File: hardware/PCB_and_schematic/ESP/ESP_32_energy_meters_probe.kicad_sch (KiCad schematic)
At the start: 33 parts, among them J2 EXTERNAL_SIGNALS, J5 METER_GRID, J9 METER_PV, U4 ST485EBDR, U5 ST485EBDR, U6 74HC14

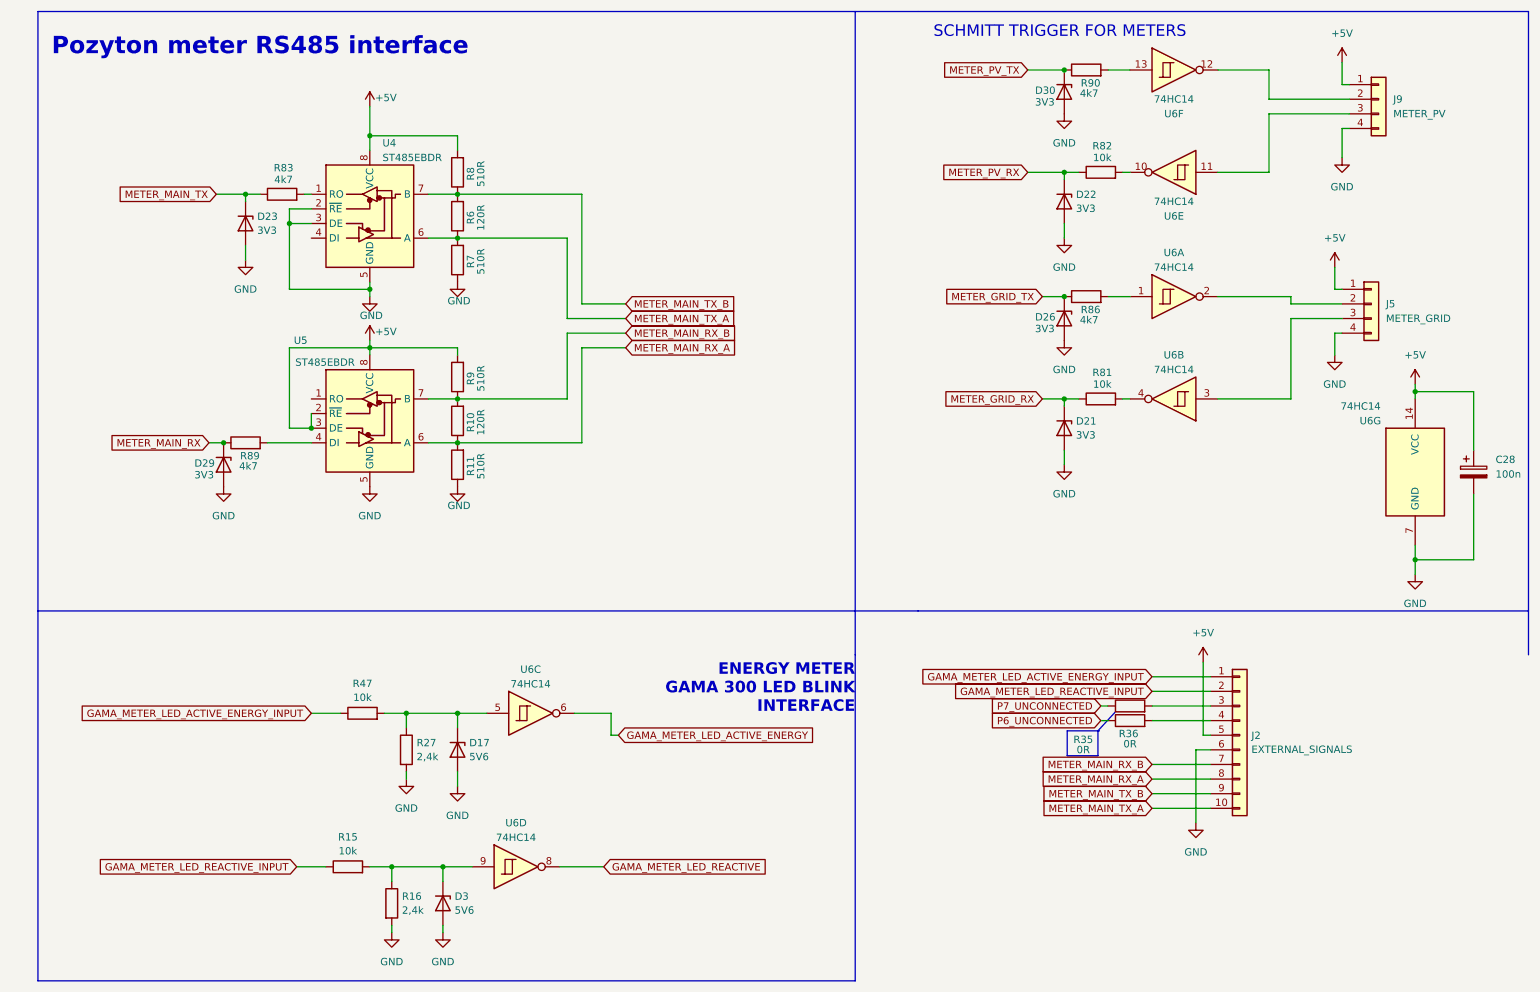
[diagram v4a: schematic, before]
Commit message: ESP PCB Route progress
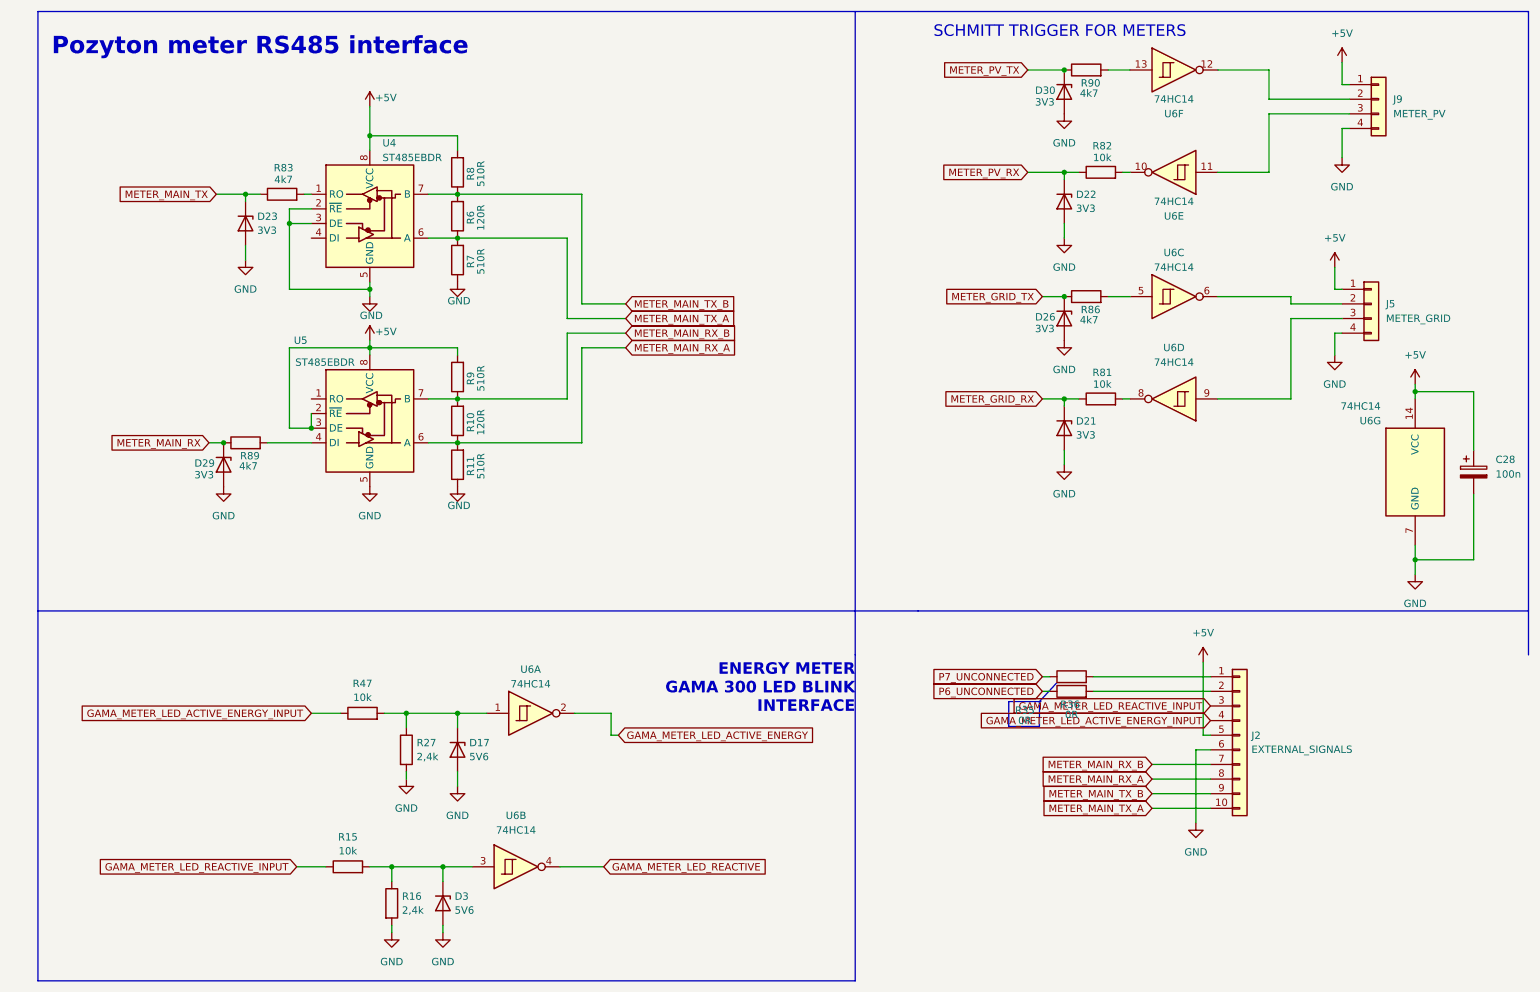
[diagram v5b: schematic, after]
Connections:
- net GAMA_METER_LED_ACTIVE_ENERGY: now also U6.2; no longer U6.6
- net GAMA_METER_LED_ACTIVE_ENERGY_INPUT: now also J2.4 (Pin_4); no longer J2.1 (Pin_1)
- net GAMA_METER_LED_REACTIVE: now also U6.4; no longer U6.8
- net GAMA_METER_LED_REACTIVE_INPUT: now also J2.3 (Pin_3); no longer J2.2 (Pin_2)
- net at D17.1 (K), R27.1, R47.2: now also U6.1; no longer U6.5
- net at R35.2: now also J2.1 (Pin_1); no longer J2.3 (Pin_3)
- net at R36.2: now also J2.2 (Pin_2); no longer J2.4 (Pin_4)
- net at U6.3: now also D3.1 (K), R15.2, R16.1; no longer J5.3 (Pin_3)
- net at R81.2: now also U6.8; no longer U6.4
- net at R86.2: now also U6.5; no longer U6.1
- net at J5.2 (Pin_2): now also U6.6; no longer U6.2
- new net: J5.3 (Pin_3), U6.9
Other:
- moved on the sheet: R35, R36, U6A, U6B, U6C, U6D
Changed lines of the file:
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@@
 	(wire
 		(pts
-			(xy 215.9 140.97) (xy 226.06 140.97)
-		)
-		(stroke
-			(width 0)
-			(type default)
-		)
-	)
-	(wire
-		(pts
 			(xy 236.22 45.72) (xy 227.33 45.72)
 		)
@@
 	(wire
 		(pts
-			(xy 215.9 133.35) (xy 226.06 133.35)
+			(xy 205.74 133.35) (xy 226.06 133.35)
 		)
 		(stroke
@@
 	(wire
 		(pts
-			(xy 215.9 138.43) (xy 226.06 138.43)
-		)
-		(stroke
-			(width 0)
-			(type default)
-		)
-	)
-	(wire
-		(pts
 			(xy 58.42 58.42) (xy 58.42 60.96)
 		)
@@
 	(wire
 		(pts
-			(xy 207.01 140.97) (xy 208.28 140.97)
+			(xy 196.85 135.89) (xy 198.12 135.89)
 		)
 		(stroke
@@
 	(polyline
 		(pts
-			(xy 206.502 142.748) (xy 209.55 139.446)
+			(xy 196.342 137.668) (xy 199.39 134.366)
 		)
 		(stroke
@@
 	(wire
 		(pts
-			(xy 207.01 138.43) (xy 208.28 138.43)
+			(xy 196.85 133.35) (xy 198.12 133.35)
 		)
 		(stroke
@@
 	(polyline
 		(pts
-			(xy 206.756 142.748) (xy 206.502 142.748)
+			(xy 196.596 137.668) (xy 196.342 137.668)
 		)
 		(stroke
@@
 	(wire
 		(pts
-			(xy 215.9 135.89) (xy 226.06 135.89)
+			(xy 205.74 135.89) (xy 226.06 135.89)
 		)
 		(stroke
@@
 	)
 	(rectangle
-		(start 201.168 142.748)
-		(end 206.502 147.066)
+		(start 191.008 137.668)
+		(end 196.342 141.986)
 		(stroke
 			(width 0)
@@
 	(global_label "GAMA_METER_LED_ACTIVE_ENERGY_INPUT"
 		(shape input)
-		(at 215.9 133.35 180)
+		(at 226.06 140.97 180)
 		(fields_autoplaced yes)
 		(effects
@@
 		)
 		(property "Intersheetrefs" "${INTERSHEET_REFS}"
-			(at 174.815 133.35 0)
+			(at 184.975 140.97 0)
 			(effects
 				(font
@@
 	(global_label "GAMA_METER_LED_REACTIVE_INPUT"
 		(shape input)
-		(at 215.9 135.89 180)
+		(at 226.06 138.43 180)
 		(fields_autoplaced yes)
 		(effects
@@
 		)
 		(property "Intersheetrefs" "${INTERSHEET_REFS}"
-			(at 180.6207 135.89 0)
+			(at 190.7807 138.43 0)
 			(effects
 				(font
@@
 	(global_label "P7_UNCONNECTED"
 		(shape input)
-		(at 207.01 138.43 180)
+		(at 196.85 133.35 180)
 		(fields_autoplaced yes)
 		(effects
@@
 		)
 		(property "Intersheetrefs" "${INTERSHEET_REFS}"
-			(at 186.8496 138.43 0)
+			(at 176.6896 133.35 0)
 			(effects
 				(font
@@
 	(global_label "P6_UNCONNECTED"
 		(shape input)
-		(at 207.01 140.97 180)
+		(at 196.85 135.89 180)
 		(fields_autoplaced yes)
 		(effects
@@
 		)
 		(property "Intersheetrefs" "${INTERSHEET_REFS}"
-			(at 186.8496 140.97 0)
+			(at 176.6896 135.89 0)
 			(effects
 				(font
@@
 	(symbol
 		(lib_id "74xx:74HC14")
-		(at 219.71 85.09 180)
+		(at 105.41 166.37 0)
 		(unit 2)
 		(exclude_from_sim no)
@@
 		(fields_autoplaced yes)
 		(property "Reference" "U6"
-			(at 219.71 77.47 0)
+			(at 105.41 157.48 0)
 			(effects
 				(font
@@
 		)
 		(property "Value" "74HC14"
-			(at 219.71 80.01 0)
+			(at 105.41 160.02 0)
 			(effects
 				(font
@@
 		)
 		(property "Footprint" "Package_SO:SOIC-14_3.9x8.7mm_P1.27mm"
-			(at 219.71 85.09 0)
+			(at 105.41 166.37 0)
 			(effects
 				(font
@@
 		)
 		(property "Datasheet" "http://www.ti.com/lit/gpn/sn74HC14"
-			(at 219.71 85.09 0)
+			(at 105.41 166.37 0)
 			(effects
 				(font
@@
 		)
 		(property "Description" "Hex inverter schmitt trigger"
-			(at 219.71 85.09 0)
+			(at 105.41 166.37 0)
 			(effects
 				(font
@@
 	(symbol
 		(lib_id "74xx:74HC14")
-		(at 107.95 139.7 0)
+		(at 219.71 67.31 0)
 		(unit 3)
 		(exclude_from_sim no)
@@
 		(fields_autoplaced yes)
 		(property "Reference" "U6"
-			(at 107.95 132.08 0)
+			(at 219.71 59.69 0)
 			(effects
 				(font
@@
 		)
 		(property "Value" "74HC14"
-			(at 107.95 134.62 0)
+			(at 219.71 62.23 0)
 			(effects
 				(font
@@
 		)
 		(property "Footprint" "Package_SO:SOIC-14_3.9x8.7mm_P1.27mm"
-			(at 107.95 139.7 0)
+			(at 219.71 67.31 0)
 			(effects
 				(font
@@
 		)
 		(property "Datasheet" "http://www.ti.com/lit/gpn/sn74HC14"
-			(at 107.95 139.7 0)
+			(at 219.71 67.31 0)
 			(effects
 				(font
@@
 		)
 		(property "Description" "Hex inverter schmitt trigger"
-			(at 107.95 139.7 0)
+			(at 219.71 67.31 0)
 			(effects
 				(font
@@
 	(symbol
 		(lib_id "74xx:74HC14")
-		(at 105.41 166.37 0)
+		(at 219.71 85.09 180)
 		(unit 4)
 		(exclude_from_sim no)
@@
 		(fields_autoplaced yes)
 		(property "Reference" "U6"
-			(at 105.41 158.75 0)
+			(at 219.71 76.2 0)
 			(effects
 				(font
@@
 		)
 		(property "Value" "74HC14"
-			(at 105.41 161.29 0)
+			(at 219.71 78.74 0)
 			(effects
 				(font
@@
 		)
 		(property "Footprint" "Package_SO:SOIC-14_3.9x8.7mm_P1.27mm"
-			(at 105.41 166.37 0)
+			(at 219.71 85.09 0)
 			(effects
 				(font
@@
 		)
 		(property "Datasheet" "http://www.ti.com/lit/gpn/sn74HC14"
-			(at 105.41 166.37 0)
+			(at 219.71 85.09 0)
 			(effects
 				(font
@@
 		)
 		(property "Description" "Hex inverter schmitt trigger"
-			(at 105.41 166.37 0)
+			(at 219.71 85.09 0)
 			(effects
 				(font
@@
 	(symbol
 		(lib_id "Device:R")
-		(at 212.09 138.43 90)
+		(at 201.93 133.35 90)
 		(unit 1)
 		(exclude_from_sim no)
@@
 		(dnp no)
 		(property "Reference" "R35"
-			(at 203.962 144.272 90)
+			(at 193.802 139.192 90)
 			(effects
 				(font
@@
 		)
 		(property "Value" "0R"
-			(at 203.962 146.05 90)
+			(at 193.802 140.97 90)
 			(effects
 				(font
@@
 		)
 		(property "Footprint" "Resistor_SMD:R_0805_2012Metric_Pad1.20x1.40mm_HandSolder"
-			(at 212.09 140.208 90)
+			(at 201.93 135.128 90)
 			(effects
 				(font
@@
 		)
 		(property "Datasheet" "~"
-			(at 212.09 138.43 0)
+			(at 201.93 133.35 0)
 			(effects
 				(font
@@
 		)
 		(property "Description" "Resistor"
-			(at 212.09 138.43 0)
+			(at 201.93 133.35 0)
 			(effects
 				(font
@@
 	(symbol
 		(lib_id "74xx:74HC14")
-		(at 219.71 67.31 0)
+		(at 107.95 139.7 0)
 		(unit 1)
 		(exclude_from_sim no)
@@
 		(fields_autoplaced yes)
 		(property "Reference" "U6"
-			(at 219.71 59.69 0)
+			(at 107.95 132.08 0)
 			(effects
 				(font
@@
 		)
 		(property "Value" "74HC14"
-			(at 219.71 62.23 0)
+			(at 107.95 134.62 0)
 			(effects
 				(font
@@
 		)
 		(property "Footprint" "Package_SO:SOIC-14_3.9x8.7mm_P1.27mm"
-			(at 219.71 67.31 0)
+			(at 107.95 139.7 0)
 			(effects
 				(font
@@
 		)
 		(property "Datasheet" "http://www.ti.com/lit/gpn/sn74HC14"
-			(at 219.71 67.31 0)
+			(at 107.95 139.7 0)
 			(effects
 				(font
@@
 		)
 		(property "Description" "Hex inverter schmitt trigger"
-			(at 219.71 67.31 0)
+			(at 107.95 139.7 0)
 			(effects
 				(font
@@
 	(symbol
 		(lib_id "Device:R")
-		(at 212.09 140.97 90)
+		(at 201.93 135.89 90)
 		(unit 1)
 		(exclude_from_sim no)
@@
 		(dnp no)
 		(property "Reference" "R36"
-			(at 211.836 143.256 90)
+			(at 201.676 138.176 90)
 			(effects
 				(font
@@
 		)
 		(property "Value" "0R"
-			(at 212.09 145.034 90)
+			(at 201.93 139.954 90)
 			(effects
 				(font
@@
 		)
 		(property "Footprint" "Resistor_SMD:R_0805_2012Metric_Pad1.20x1.40mm_HandSolder"
-			(at 212.09 142.748 90)
+			(at 201.93 137.668 90)
 			(effects
 				(font
@@
 		)
 		(property "Datasheet" "~"
-			(at 212.09 140.97 0)
+			(at 201.93 135.89 0)
 			(effects
 				(font
@@
 		)
 		(property "Description" "Resistor"
-			(at 212.09 140.97 0)
+			(at 201.93 135.89 0)
 			(effects
 				(font

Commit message: Fineing ESP PCB
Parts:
- renumbered C28 to C18, D29 to D12, D23 to D13, D3 to D14, D17 to D15, D30 to D16, D22 to D17, D26 to D18, D21 to D19, J2 to J11, J5 to J12, J9 to J13, R89 to R42, R83 to R43, R15 to R44, R47 to R45, R16 to R46, R27 to R47, R8 to R48, R6 to R49, R7 to R50, R9 to R51, R10 to R52, R11 to R53, R35 to R54, R36 to R55, R90 to R56, R86 to R57, R82 to R58, R81 to R59, U5 to U10, U6 to U11, U4 to U9

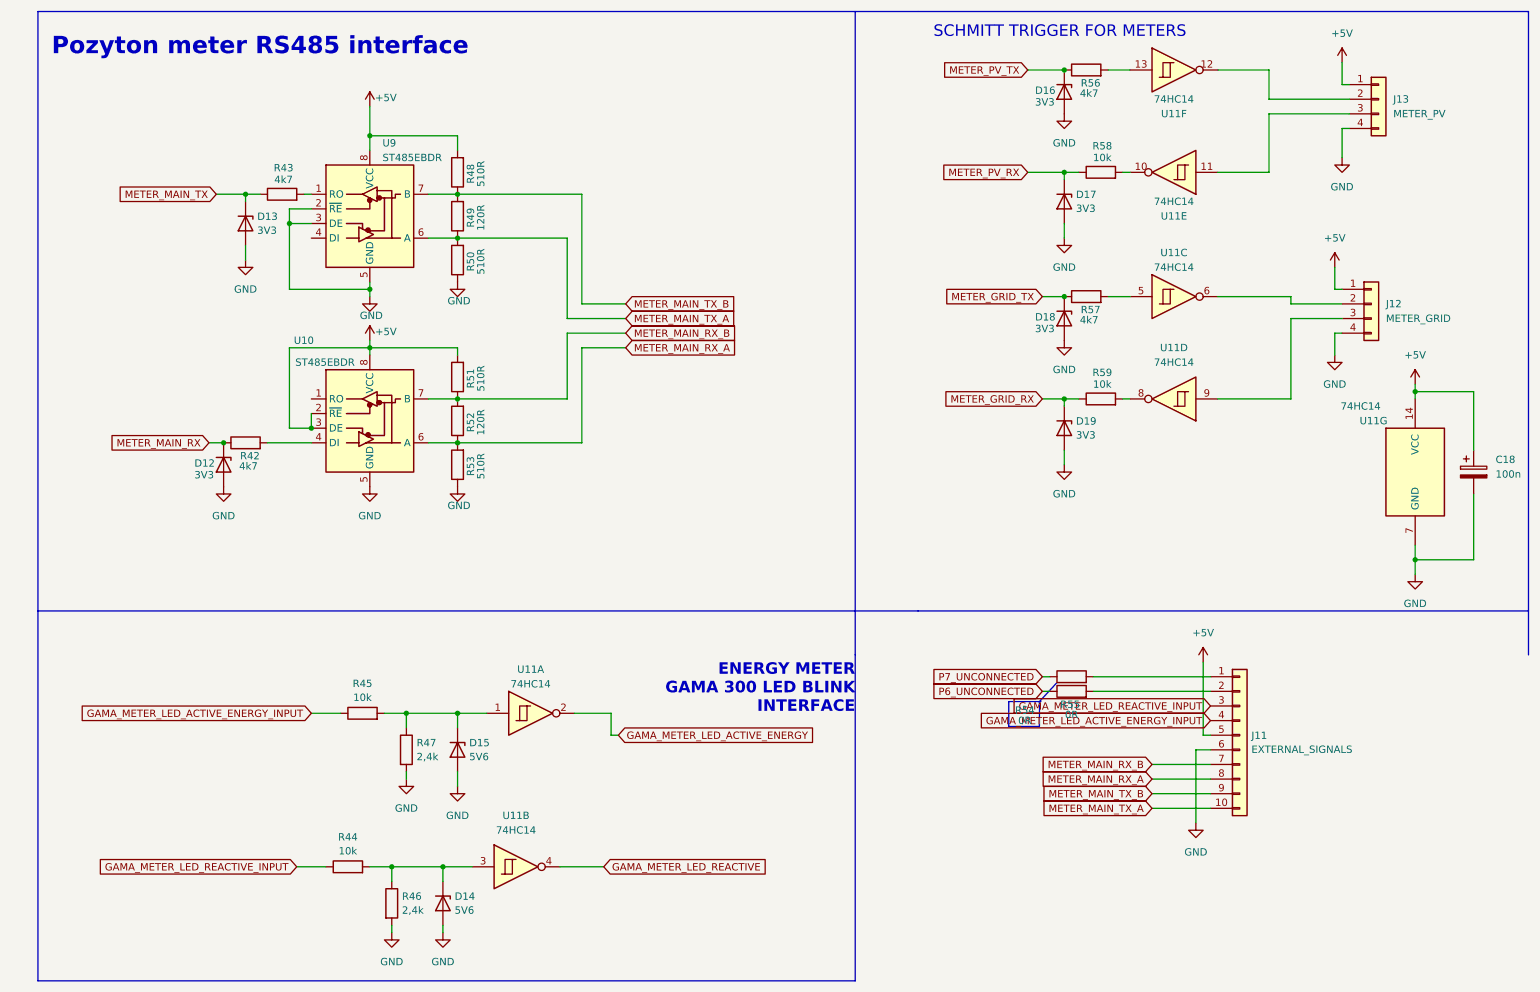
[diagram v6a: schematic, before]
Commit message: Add SD card switcher circuit, some changes in pcb and schematic
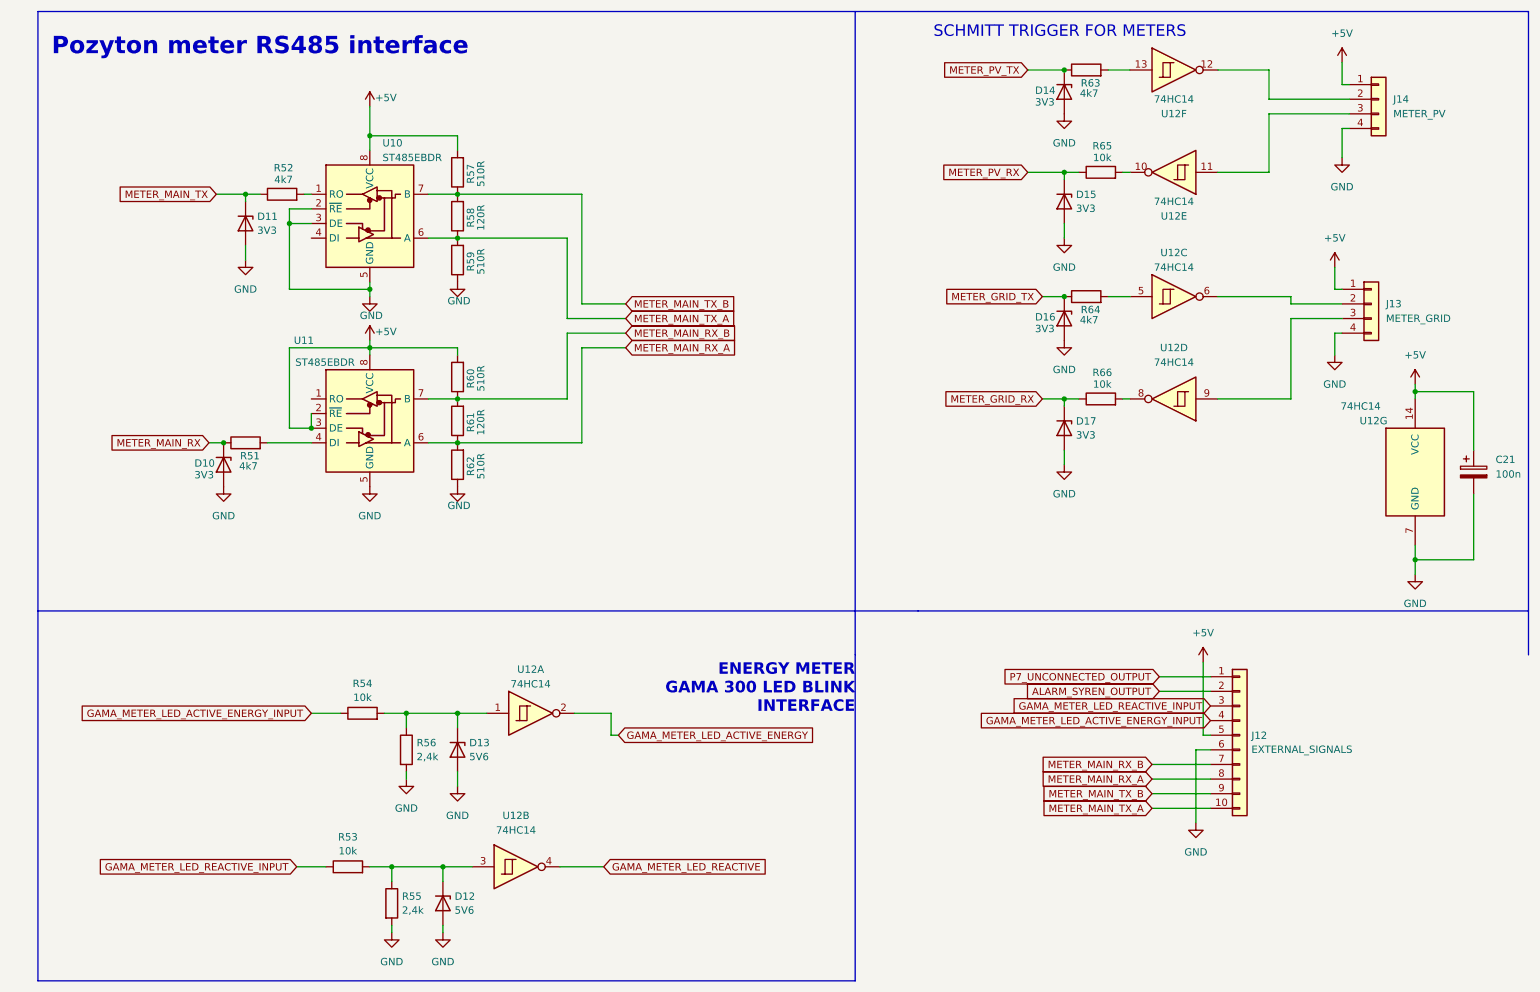
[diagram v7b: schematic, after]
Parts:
- removed R54, R55: 0R, Resistor_SMD:R_0805_2012Metric_Pad1.20x1.40mm_HandSolder, symbol Device:R
- renumbered C18 to C21, D12 to D10, D13 to D11, D14 to D12, D15 to D13, D16 to D14, D17 to D15, D18 to D16, D19 to D17, J11 to J12, J12 to J13, J13 to J14, R42 to R51, R43 to R52, R44 to R53, R45 to R54, R46 to R55, R47 to R56, R48 to R57, R49 to R58, R50 to R59, R51 to R60, R52 to R61, R53 to R62, R56 to R63, R57 to R64, R58 to R65, R59 to R66, U9 to U10, U10 to U11, U11 to U12
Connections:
- net P7_UNCONNECTED_OUTPUT: now reaches J12.1 (Pin_1)
- net ALARM_SYREN_OUTPUT: now reaches J12.2 (Pin_2)
